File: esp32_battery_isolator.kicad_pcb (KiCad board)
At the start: 4 copper layers, 90 x 89.9 mm, 100 parts, among them J1 Conn_01x03_Male, J2 USB_C_Receptacle_USB2.0, Q1 MMBT3904, Q10 MMBT3904, Q11 MMBT3906, Q12 AONR21357, Q13 MMBT3904, Q14 MMBT3904, Q15 MMBT3904, Q16 MMBT3906, Q17 MMBT3904, Q18 AONR21357, Q19 MMBT3904, Q2 MMBT3904, Q20 MMBT3906, Q21 AONR21357, Q3 MMBT3906, Q4 HSBA100P03, Q5 HSBA100P03, Q6 HSBA100P03, Q7 HSBA100P03, Q8 MMBT3904, Q9 MMBT3904, SW1 C620183, SW2 C620183, U1 ESP32-WROOM-32D, U10 INA219BxDCN, U2 INA219BxDCN, U3 INA219BxDCN, U4 INA219BxDCN, U5 XL1509_SOP8, U6 CH340N, U7 INA219BxDCN, U8 ADC128D818, U9 INA219BxDCN

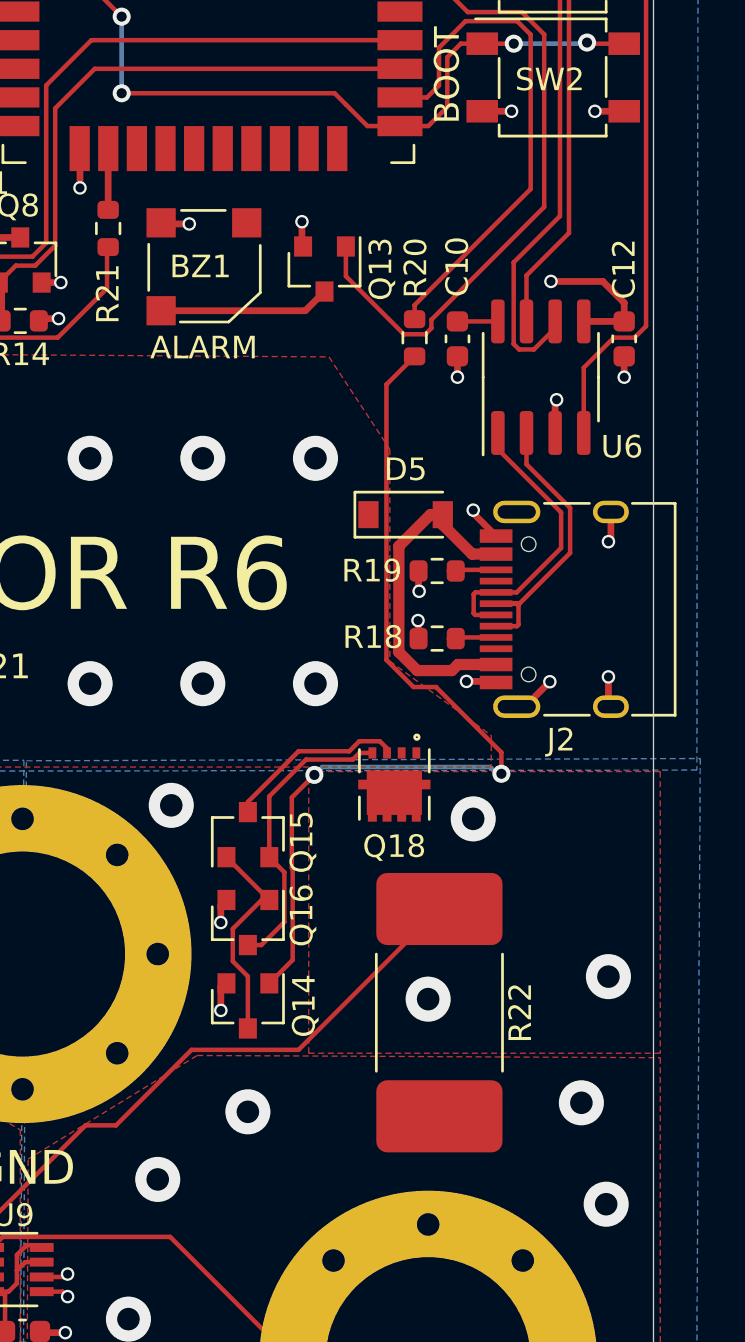
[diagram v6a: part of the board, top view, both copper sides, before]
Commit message: shipped to JLCPCB as Rev 6
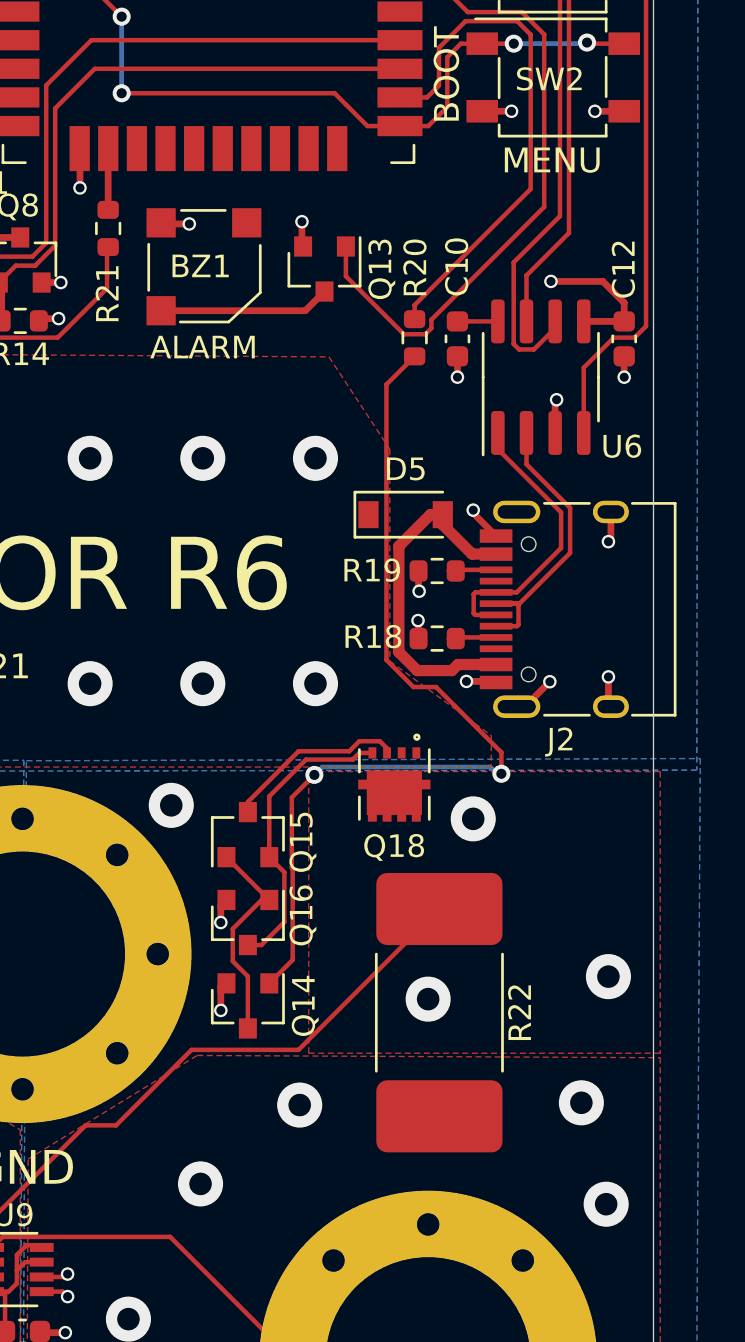
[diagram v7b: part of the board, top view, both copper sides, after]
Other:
- board text added: "MENU"
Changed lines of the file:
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@@
       (layer "B.Paste" (type "Bottom Solder Paste"))
       (layer "B.SilkS" (type "Bottom Silk Screen"))
-      (copper_finish "None")
+      (copper_finish "HAL SnPb")
       (dielectric_constraints no)
     )
@@
     (effects (font (size 1 1) (thickness 0.15)))
   )
+  (gr_text "MENU" (at 193.15 70.95) (layer "F.SilkS")
+    (effects (font (size 1.1 1.1) (thickness 0.22)))
+  )
   (gr_text "ACEA QUIGG 12/21" (at 162.8 93.4) (layer "F.SilkS")
     (effects (font (size 1.1 1.1) (thickness 0.25)))
@@
   (segment (start 168.769511 118.700489) (end 168.3 119.17) (width 0.2) (layer "F.Cu") (net 21))
   (segment (start 181.65 124.15) (end 176.200489 118.700489) (width 0.2) (layer "F.Cu") (net 21))
-  (via (at 175.65 116.15) (size 2) (drill 1) (layers "F.Cu" "B.Cu") (free) (net 21))
-  (via (at 179.65 113.15) (size 2) (drill 1) (layers "F.Cu" "B.Cu") (free) (net 21))
+  (via (at 177.55 116.35) (size 2) (drill 1) (layers "F.Cu" "B.Cu") (free) (net 21))
+  (via (at 181.95 112.85) (size 2) (drill 1) (layers "F.Cu" "B.Cu") (free) (net 21))
   (via (at 194.45 112.75) (size 2) (drill 1) (layers "F.Cu" "B.Cu") (free) (net 21))
   (via (at 181.25 132.15) (size 2) (drill 1) (layers "F.Cu" "B.Cu") (free) (net 21))
